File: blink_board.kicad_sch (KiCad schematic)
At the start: 25 parts, among them J1 USB_C_Receptacle_PowerOnly_6P, J2 Debug, SW1 BTN_1, SW2 BTN_2, U1 ESP-01v090, U2 MIC5504-3.3YM5, U3 MCP23017_SO

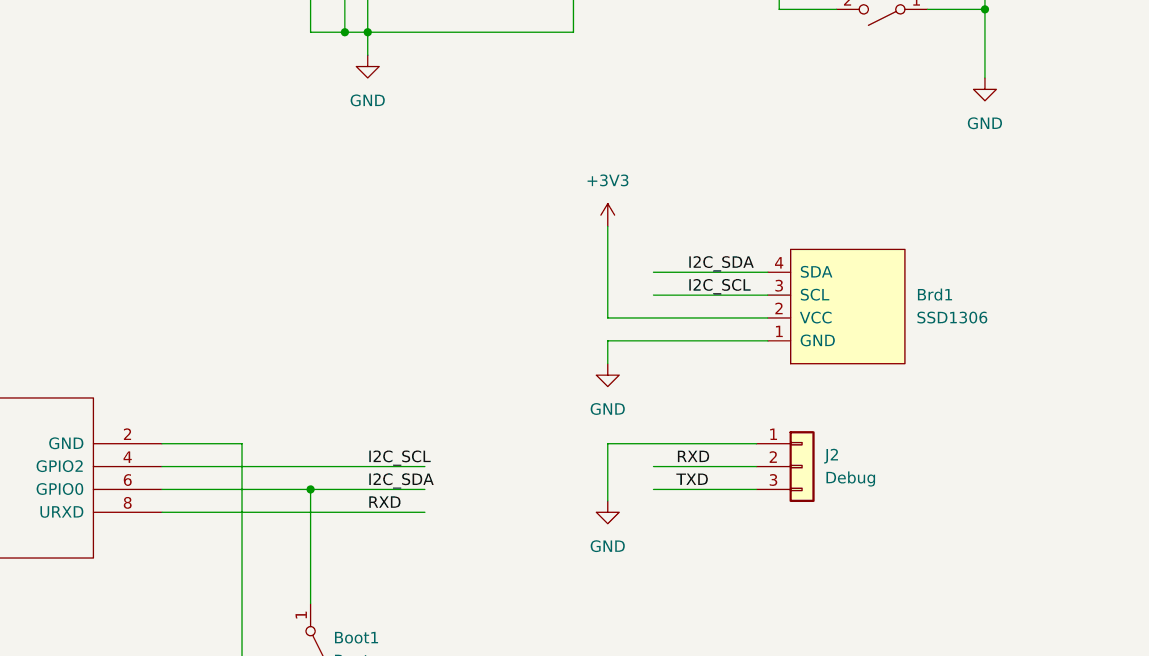
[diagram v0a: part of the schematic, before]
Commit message: Bugfixes and updates
* Added small board description
* Added testpads for I2C
* Fixed power for display
* Added labels for Serial
* Aligned buttons
* Cleaned silkscreen
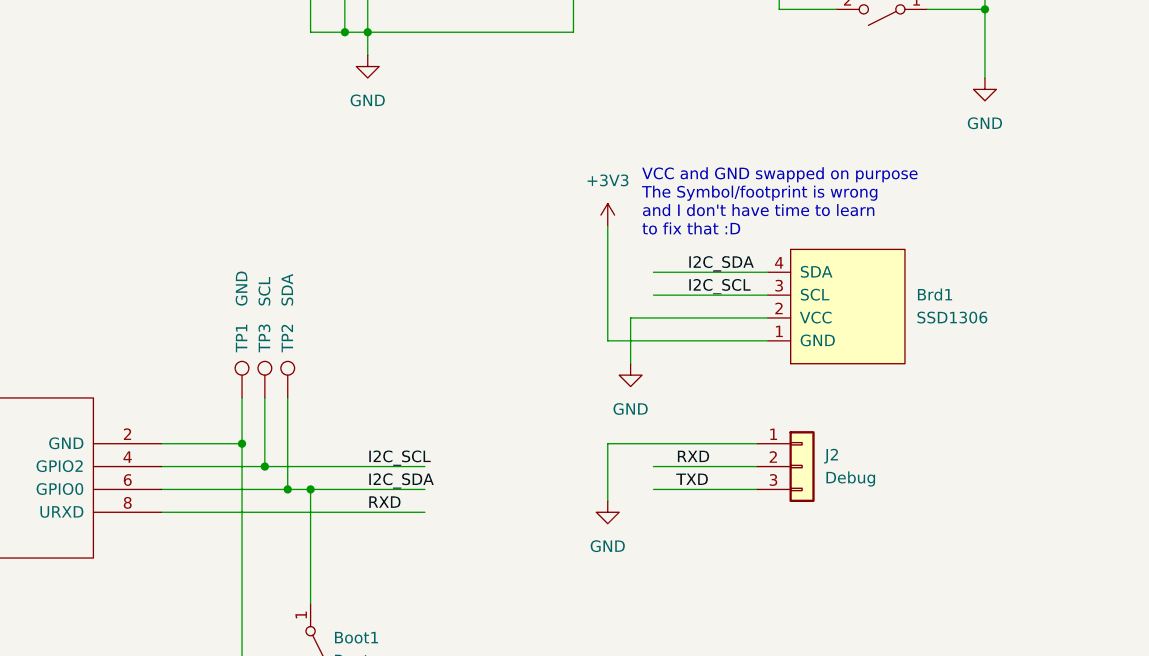
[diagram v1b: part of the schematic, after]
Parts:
- added TP1: GND, TestPoint:TestPoint_Pad_D1.5mm, symbol Connector:TestPoint
- added TP2: SDA, TestPoint:TestPoint_Pad_D1.5mm, symbol Connector:TestPoint
- added TP3: SCL, TestPoint:TestPoint_Pad_D1.5mm, symbol Connector:TestPoint
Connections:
- net +3V3: now also Brd1.1 (GND); no longer Brd1.2 (VCC)
- net GND: now also Brd1.2 (VCC), TP1.1; no longer Brd1.1 (GND)
- net I2C_SCL: now also TP3.1
- net I2C_SDA: now also TP2.1
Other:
- note added: "VCC and GND swapped on purpose The Symbol/footprint is wrong and I don't have time to learn to fix that :D"
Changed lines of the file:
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@@
   (junction (at 107.95 31.75) (diameter 0) (color 0 0 0 0)
   )
+  (junction (at 132.08 151.13) (diameter 0) (color 0 0 0 0)
+  )
   (junction (at 228.6 63.5) (diameter 0) (color 0 0 0 0)
   )
@@
   )
   (junction (at 228.6 29.21) (diameter 0) (color 0 0 0 0)
+  )
+  (junction (at 129.54 148.59) (diameter 0) (color 0 0 0 0)
+  )
+  (junction (at 134.62 153.67) (diameter 0) (color 0 0 0 0)
   )
   (no_connect (at 148.59 66.04))
@@
   (no_connect (at 184.15 60.96))
   (no_connect (at 184.15 83.82))
-  (wire (pts (xy 187.96 137.16) (xy 170.18 137.16))
+  (wire (pts (xy 134.62 153.67) (xy 137.16 153.67))
     (stroke (width 0) (type default))
   )
@@
     (stroke (width 0) (type default))
   )
-  (wire (pts (xy 170.18 134.62) (xy 170.18 124.46))
+  (wire (pts (xy 170.18 124.46) (xy 170.18 137.16))
     (stroke (width 0) (type default))
   )
@@
     (stroke (width 0) (type default))
   )
+  (wire (pts (xy 132.08 143.51) (xy 132.08 151.13))
+    (stroke (width 0) (type default))
+  )
   (wire (pts (xy 166.37 21.59) (xy 157.48 21.59))
     (stroke (width 0) (type default))
@@
     (stroke (width 0) (type default))
   )
-  (wire (pts (xy 170.18 137.16) (xy 170.18 139.7))
-    (stroke (width 0) (type default))
-  )
   (wire (pts (xy 55.88 156.21) (xy 55.88 160.02))
     (stroke (width 0) (type default))
@@
     (stroke (width 0) (type default))
   )
+  (wire (pts (xy 172.72 134.62) (xy 187.96 134.62))
+    (stroke (width 0) (type default))
+  )
   (wire (pts (xy 184.15 55.88) (xy 196.85 55.88))
     (stroke (width 0) (type default))
@@
     (stroke (width 0) (type default))
   )
+  (wire (pts (xy 132.08 151.13) (xy 149.86 151.13))
+    (stroke (width 0) (type default))
+  )
   (wire (pts (xy 222.25 40.64) (xy 228.6 40.64))
     (stroke (width 0) (type default))
   )
-  (wire (pts (xy 187.96 134.62) (xy 170.18 134.62))
-    (stroke (width 0) (type default))
-  )
   (wire (pts (xy 140.97 71.12) (xy 148.59 71.12))
     (stroke (width 0) (type default))
@@
     (stroke (width 0) (type default))
   )
+  (wire (pts (xy 129.54 143.51) (xy 129.54 148.59))
+    (stroke (width 0) (type default))
+  )
   (wire (pts (xy 91.44 41.91) (xy 91.44 45.72))
     (stroke (width 0) (type default))
@@
     (stroke (width 0) (type default))
   )
-  (wire (pts (xy 120.65 151.13) (xy 149.86 151.13))
+  (wire (pts (xy 120.65 151.13) (xy 132.08 151.13))
     (stroke (width 0) (type default))
   )
@@
     (stroke (width 0) (type default))
   )
-  (wire (pts (xy 120.65 153.67) (xy 137.16 153.67))
+  (wire (pts (xy 120.65 153.67) (xy 134.62 153.67))
     (stroke (width 0) (type default))
   )
@@
     (stroke (width 0) (type default))
   )
+  (wire (pts (xy 170.18 137.16) (xy 187.96 137.16))
+    (stroke (width 0) (type default))
+  )
   (wire (pts (xy 91.44 45.72) (xy 107.95 45.72))
     (stroke (width 0) (type default))
@@
     (stroke (width 0) (type default))
   )
+  (wire (pts (xy 134.62 143.51) (xy 134.62 153.67))
+    (stroke (width 0) (type default))
+  )
   (wire (pts (xy 196.85 63.5) (xy 201.93 63.5))
     (stroke (width 0) (type default))
@@
     (stroke (width 0) (type default))
   )
+  (wire (pts (xy 172.72 134.62) (xy 172.72 139.7))
+    (stroke (width 0) (type default))
+  )
   (wire (pts (xy 209.55 63.5) (xy 214.63 63.5))
     (stroke (width 0) (type default))
@@
   (wire (pts (xy 189.23 73.66) (xy 189.23 100.33))
     (stroke (width 0) (type default))
+  )
+  (text "VCC and GND swapped on purpose\nThe Symbol/footprint is wrong\nand I don't have time to learn\nto fix that :D"
+    (at 173.99 125.73 0)
+    (effects (font (size 1.27 1.27)) (justify left bottom))
   )
   (label "I2C_SCL" (at 137.16 50.8 0) (fields_autoplaced)
@@
     )
   )
-  (symbol (lib_id "power:GND") (at 170.18 139.7 0) (unit 1)
-    (in_bom yes) (on_board yes) (dnp no) (fields_autoplaced)
-    (property "Reference" "#PWR013" (at 170.18 146.05 0)
-      (effects (font (size 1.27 1.27)) hide)
-    )
-    (property "Value" "GND" (at 170.18 144.78 0)
-      (effects (font (size 1.27 1.27)))
-    )
-    (property "Footprint" "" (at 170.18 139.7 0)
-      (effects (font (size 1.27 1.27)) hide)
-    )
-    (property "Datasheet" "" (at 170.18 139.7 0)
+  (symbol (lib_id "power:GND") (at 172.72 139.7 0) (unit 1)
+    (in_bom yes) (on_board yes) (dnp no) (fields_autoplaced)
+    (property "Reference" "#PWR013" (at 172.72 146.05 0)
+      (effects (font (size 1.27 1.27)) hide)
+    )
+    (property "Value" "GND" (at 172.72 144.78 0)
+      (effects (font (size 1.27 1.27)))
+    )
+    (property "Footprint" "" (at 172.72 139.7 0)
+      (effects (font (size 1.27 1.27)) hide)
+    )
+    (property "Datasheet" "" (at 172.72 139.7 0)
       (effects (font (size 1.27 1.27)) hide)
     )
@@
     )
   )
+  (symbol (lib_id "Connector:TestPoint") (at 132.08 143.51 0) (mirror y) (unit 1)
+    (in_bom yes) (on_board yes) (dnp no)
+    (property "Reference" "TP3" (at 132.08 138.43 90)
+      (effects (font (size 1.27 1.27)) (justify left))
+    )
+    (property "Value" "SCL" (at 132.08 133.35 90)
+      (effects (font (size 1.27 1.27)) (justify left))
+    )
+    (property "Footprint" "TestPoint:TestPoint_Pad_D1.5mm" (at 127 143.51 0)
+      (effects (font (size 1.27 1.27)) hide)
+    )
+    (property "Datasheet" "~" (at 127 143.51 0)
+      (effects (font (size 1.27 1.27)) hide)
+    )
+    (pin "1")
+    (instances
+      (project "blink_board"
+        (path "/a8202eee-a8ce-464a-b159-adde84e22343"
+          (reference "TP3") (unit 1)
+        )
+      )
+    )
+  )
   (symbol (lib_id "Switch:SW_SPST") (at 200.66 100.33 180) (unit 1)
     (in_bom yes) (on_board yes) (dnp no) (fields_autoplaced)
@@
     )
   )
+  (symbol (lib_id "Connector:TestPoint") (at 134.62 143.51 0) (mirror y) (unit 1)
+    (in_bom yes) (on_board yes) (dnp no)
+    (property "Reference" "TP2" (at 134.62 138.43 90)
+      (effects (font (size 1.27 1.27)) (justify left))
+    )
+    (property "Value" "SDA" (at 134.62 133.35 90)
+      (effects (font (size 1.27 1.27)) (justify left))
+    )
+    (property "Footprint" "TestPoint:TestPoint_Pad_D1.5mm" (at 129.54 143.51 0)
+      (effects (font (size 1.27 1.27)) hide)
+    )
+    (property "Datasheet" "~" (at 129.54 143.51 0)
+      (effects (font (size 1.27 1.27)) hide)
+    )
+    (pin "1")
+    (instances
+      (project "blink_board"
+        (path "/a8202eee-a8ce-464a-b159-adde84e22343"
+          (reference "TP2") (unit 1)
+        )
+      )
+    )
+  )
   (symbol (lib_id "Device:R") (at 205.74 52.07 90) (unit 1)
     (in_bom yes) (on_board yes) (dnp no) (fields_autoplaced)
@@
         )
       )
+    )
+  )
+  (symbol (lib_id "Connector:TestPoint") (at 129.54 143.51 0) (mirror y) (unit 1)
+    (in_bom yes) (on_board yes) (dnp no)
+    (property "Reference" "TP1" (at 129.54 138.43 90)
+      (effects (font (size 1.27 1.27)) (justify left))
+    )
+    (property "Value" "GND" (at 129.54 133.35 90)
+      (effects (font (size 1.27 1.27)) (justify left))
+    )
+    (property "Footprint" "TestPoint:TestPoint_Pad_D1.5mm" (at 124.46 143.51 0)
+      (effects (font (size 1.27 1.27)) hide)
+    )
+    (property "Datasheet" "~" (at 124.46 143.51 0)
+      (effects (font (size 1.27 1.27)) hide)
+    )
+    (pin "1")
+    (instances
+      (project "blink_board"
+        (path "/a8202eee-a8ce-464a-b159-adde84e22343"
+          (reference "TP1") (unit 1)
+        )
+      )
